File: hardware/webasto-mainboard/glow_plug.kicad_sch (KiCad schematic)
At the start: 23 parts, among them Q10 SSM3J374R, Q11 2N7002, Q12 SUD50P04-08, Q13 SUD50P04-08, Q14 SUD50P04-08, Q15 SUD50P04-08, Q16 SUD50P04-08, Q17 2N7002, Q18 2N7002, U6 LM7805_TO220, U7 INA219BxDCN

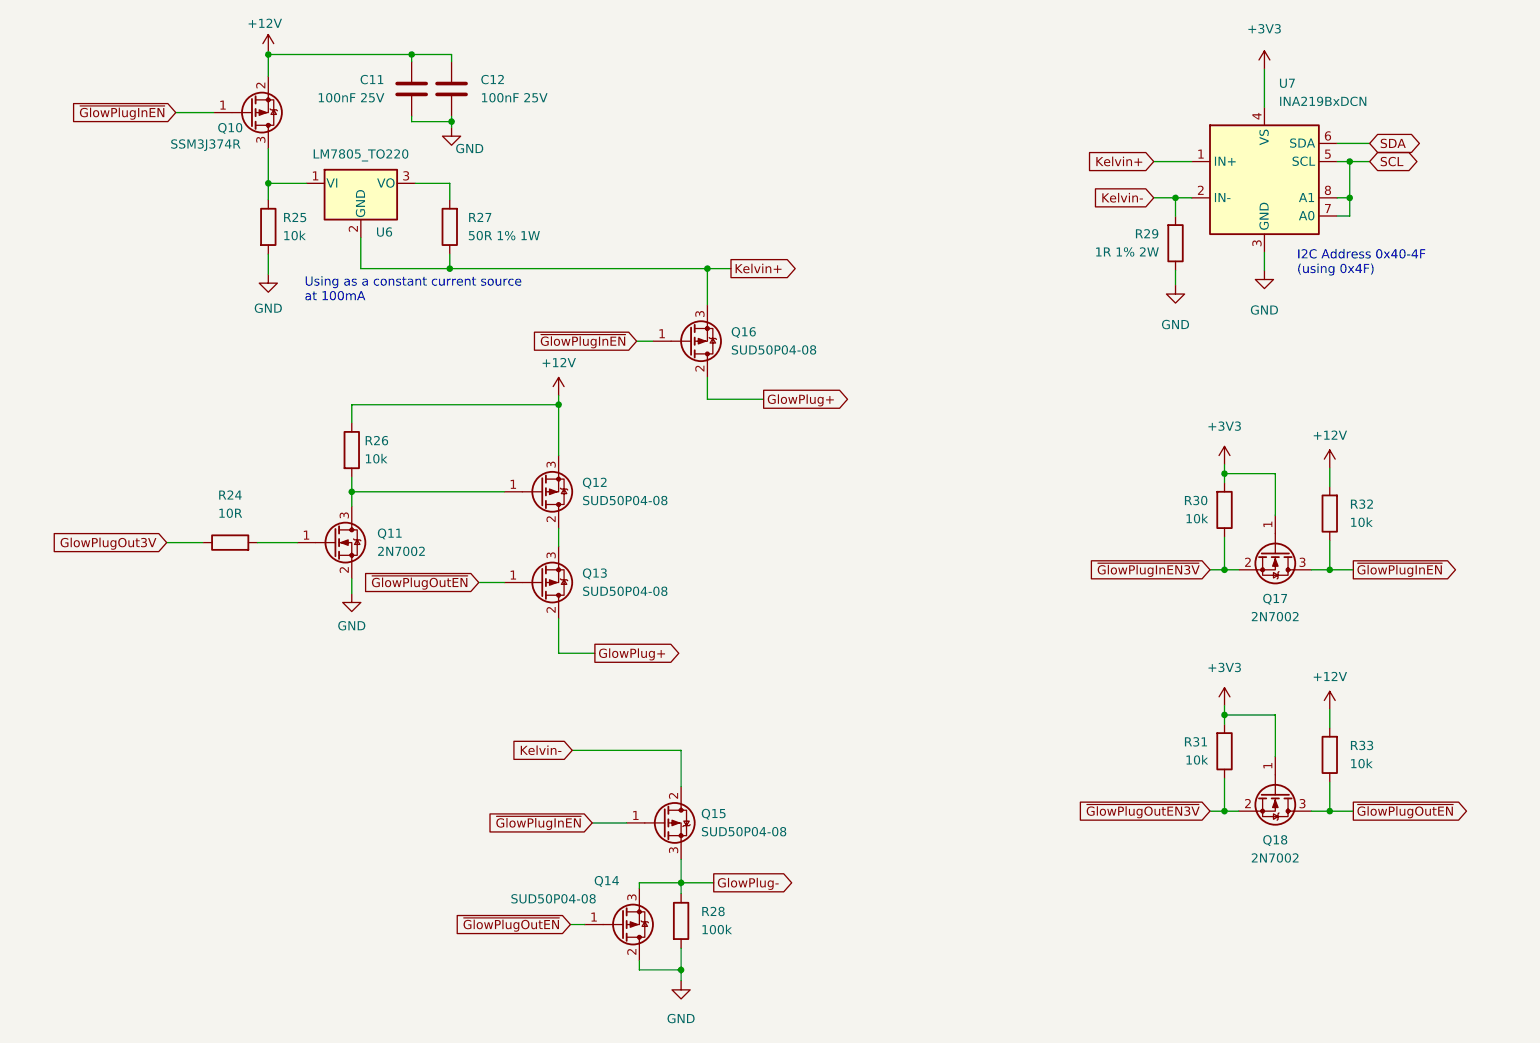
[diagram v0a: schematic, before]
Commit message: Oops.  StartRun is active at +12V.  Change the level translation.
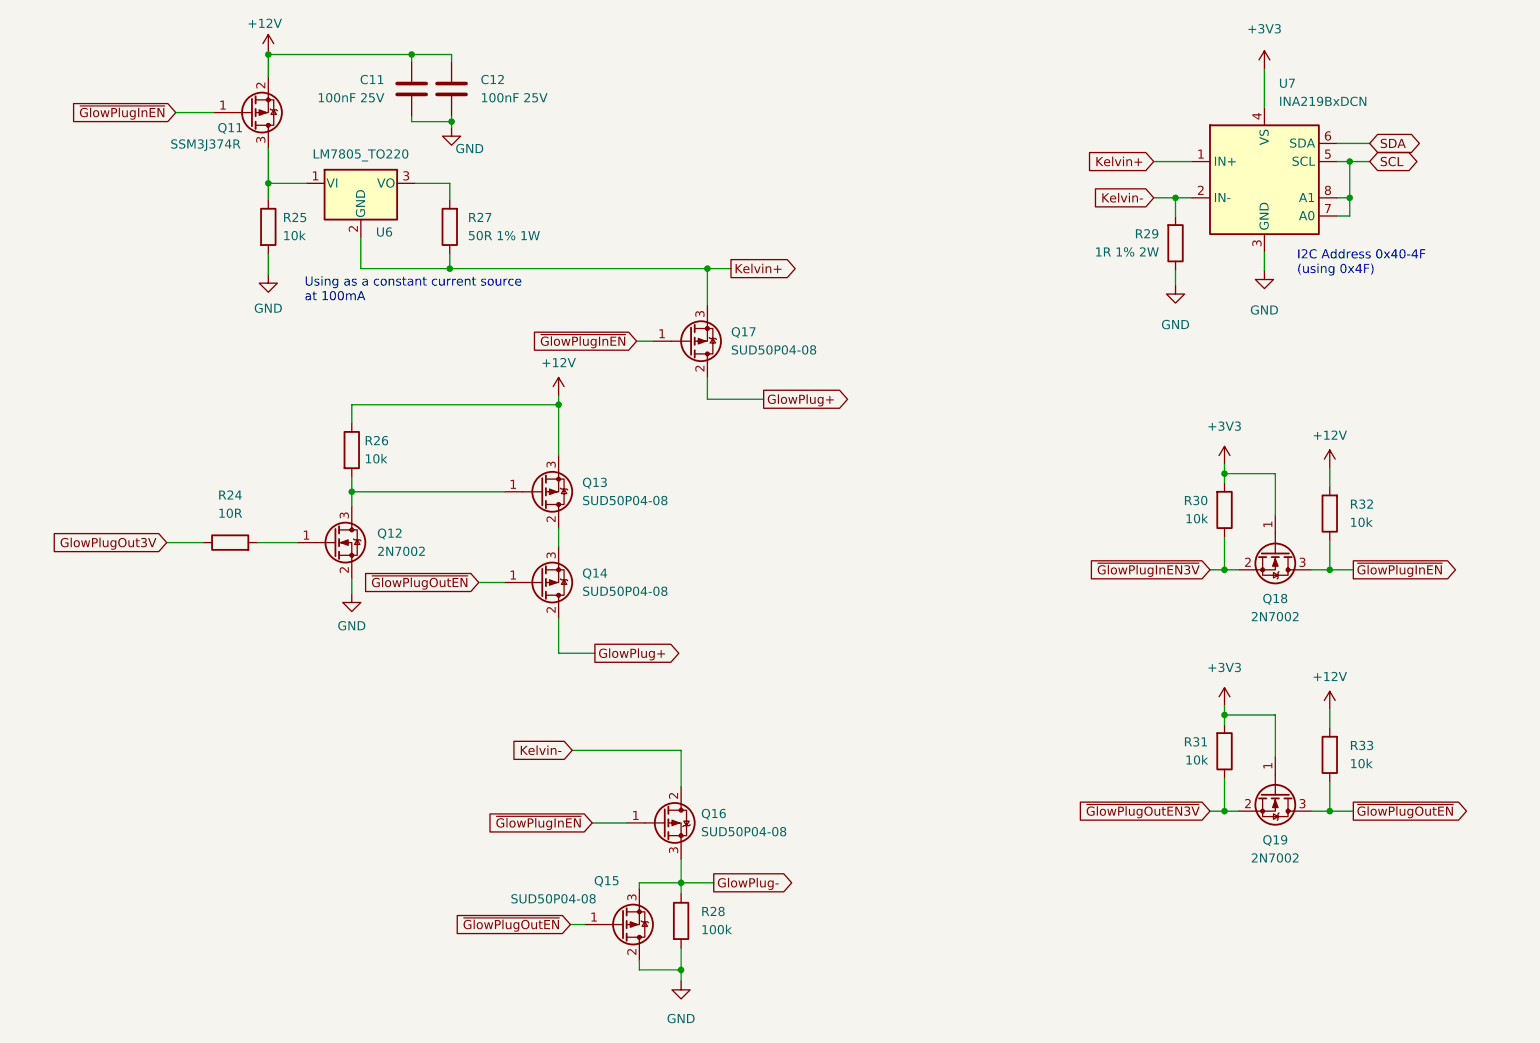
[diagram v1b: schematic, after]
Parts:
- renumbered Q10 to Q11, Q11 to Q12, Q12 to Q13, Q13 to Q14, Q14 to Q15, Q15 to Q16, Q16 to Q17, Q17 to Q18, Q18 to Q19
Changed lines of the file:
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@@
   (symbol (lib_id "Transistor_FET:2N7002") (at 204.089 97.536 270) (unit 1)
     (in_bom yes) (on_board yes) (fields_autoplaced)
-    (property "Reference" "Q17" (id 0) (at 204.089 104.14 90))
+    (property "Reference" "Q18" (id 0) (at 204.089 104.14 90))
     (property "Value" "2N7002" (id 1) (at 204.089 106.68 90))
     (property "Footprint" "Package_TO_SOT_SMD:SOT-23" (id 2) (at 202.184 102.616 0)
@@
   (symbol (lib_name "+3V3_1") (lib_id "power:+3V3") (at 202.565 29.972 0) (unit 1)
     (in_bom yes) (on_board yes) (fields_autoplaced)
-    (property "Reference" "#PWR062" (id 0) (at 202.565 33.782 0)
+    (property "Reference" "#PWR063" (id 0) (at 202.565 33.782 0)
       (effects (font (size 1.27 1.27)) hide)
     )
@@
   (symbol (lib_name "GND_8") (lib_id "power:GND") (at 202.565 58.166 0) (unit 1)
     (in_bom yes) (on_board yes) (fields_autoplaced)
-    (property "Reference" "#PWR063" (id 0) (at 202.565 64.516 0)
+    (property "Reference" "#PWR064" (id 0) (at 202.565 64.516 0)
       (effects (font (size 1.27 1.27)) hide)
     )
@@
   (symbol (lib_id "Transistor_FET:SUD50P04-08") (at 122.047 68.072 0) (mirror x) (unit 1)
     (in_bom yes) (on_board yes) (fields_autoplaced)
-    (property "Reference" "Q16" (id 0) (at 127.889 66.8019 0)
+    (property "Reference" "Q17" (id 0) (at 127.889 66.8019 0)
       (effects (font (size 1.27 1.27)) (justify left))
     )
@@
   (symbol (lib_name "+3V3_2") (lib_id "power:+3V3") (at 196.977 85.344 0) (unit 1)
     (in_bom yes) (on_board yes) (fields_autoplaced)
-    (property "Reference" "#PWR060" (id 0) (at 196.977 89.154 0)
+    (property "Reference" "#PWR061" (id 0) (at 196.977 89.154 0)
       (effects (font (size 1.27 1.27)) hide)
     )
@@
   (symbol (lib_name "GND_2") (lib_id "power:GND") (at 74.803 103.378 0) (unit 1)
     (in_bom yes) (on_board yes) (fields_autoplaced)
-    (property "Reference" "#PWR055" (id 0) (at 74.803 109.728 0)
+    (property "Reference" "#PWR056" (id 0) (at 74.803 109.728 0)
       (effects (font (size 1.27 1.27)) hide)
     )
@@
   (symbol (lib_name "+3V3_2") (lib_id "power:+3V3") (at 196.977 119.126 0) (unit 1)
     (in_bom yes) (on_board yes) (fields_autoplaced)
-    (property "Reference" "#PWR061" (id 0) (at 196.977 122.936 0)
+    (property "Reference" "#PWR062" (id 0) (at 196.977 122.936 0)
       (effects (font (size 1.27 1.27)) hide)
     )
@@
   (symbol (lib_id "Transistor_FET:SUD50P04-08") (at 118.364 135.509 0) (unit 1)
     (in_bom yes) (on_board yes) (fields_autoplaced)
-    (property "Reference" "Q15" (id 0) (at 123.698 134.2389 0)
+    (property "Reference" "Q16" (id 0) (at 123.698 134.2389 0)
       (effects (font (size 1.27 1.27)) (justify left))
     )
@@
   (symbol (lib_id "Transistor_FET:2N7002") (at 204.089 131.318 270) (unit 1)
     (in_bom yes) (on_board yes) (fields_autoplaced)
-    (property "Reference" "Q18" (id 0) (at 204.089 137.922 90))
+    (property "Reference" "Q19" (id 0) (at 204.089 137.922 90))
     (property "Value" "2N7002" (id 1) (at 204.089 140.462 90))
     (property "Footprint" "Package_TO_SOT_SMD:SOT-23" (id 2) (at 202.184 136.398 0)
@@
   (symbol (lib_name "GND_9") (lib_id "power:GND") (at 120.904 157.607 0) (unit 1)
     (in_bom yes) (on_board yes) (fields_autoplaced)
-    (property "Reference" "#PWR058" (id 0) (at 120.904 163.957 0)
+    (property "Reference" "#PWR059" (id 0) (at 120.904 163.957 0)
       (effects (font (size 1.27 1.27)) hide)
     )
@@
   (symbol (lib_name "+12V_3") (lib_id "power:+12V") (at 211.709 85.852 0) (unit 1)
     (in_bom yes) (on_board yes) (fields_autoplaced)
-    (property "Reference" "#PWR064" (id 0) (at 211.709 89.662 0)
+    (property "Reference" "#PWR065" (id 0) (at 211.709 89.662 0)
       (effects (font (size 1.27 1.27)) hide)
     )
@@
   (symbol (lib_name "GND_5") (lib_id "power:GND") (at 88.773 38.1 0) (unit 1)
     (in_bom yes) (on_board yes)
-    (property "Reference" "#PWR056" (id 0) (at 88.773 44.45 0)
+    (property "Reference" "#PWR057" (id 0) (at 88.773 44.45 0)
       (effects (font (size 1.27 1.27)) hide)
     )
@@
   (symbol (lib_name "GND_8") (lib_id "power:GND") (at 190.119 60.198 0) (unit 1)
     (in_bom yes) (on_board yes) (fields_autoplaced)
-    (property "Reference" "#PWR059" (id 0) (at 190.119 66.548 0)
+    (property "Reference" "#PWR060" (id 0) (at 190.119 66.548 0)
       (effects (font (size 1.27 1.27)) hide)
     )
@@
   (symbol (lib_id "Transistor_FET:SUD50P04-08") (at 101.219 89.154 0) (mirror x) (unit 1)
     (in_bom yes) (on_board yes) (fields_autoplaced)
-    (property "Reference" "Q12" (id 0) (at 107.061 87.8839 0)
+    (property "Reference" "Q13" (id 0) (at 107.061 87.8839 0)
       (effects (font (size 1.27 1.27)) (justify left))
     )
@@
   (symbol (lib_name "+12V_2") (lib_id "power:+12V") (at 63.119 27.686 0) (unit 1)
     (in_bom yes) (on_board yes)
-    (property "Reference" "#PWR053" (id 0) (at 63.119 31.496 0)
+    (property "Reference" "#PWR054" (id 0) (at 63.119 31.496 0)
       (effects (font (size 1.27 1.27)) hide)
     )
@@
   (symbol (lib_name "+12V_3") (lib_id "power:+12V") (at 211.709 119.634 0) (unit 1)
     (in_bom yes) (on_board yes) (fields_autoplaced)
-    (property "Reference" "#PWR065" (id 0) (at 211.709 123.444 0)
+    (property "Reference" "#PWR066" (id 0) (at 211.709 123.444 0)
       (effects (font (size 1.27 1.27)) hide)
     )
@@
   (symbol (lib_id "Transistor_FET:SUD50P04-08") (at 112.522 149.733 0) (mirror x) (unit 1)
     (in_bom yes) (on_board yes)
-    (property "Reference" "Q14" (id 0) (at 108.712 143.637 0)
+    (property "Reference" "Q15" (id 0) (at 108.712 143.637 0)
       (effects (font (size 1.27 1.27)) (justify left))
     )
@@
   (symbol (lib_name "GND_3") (lib_id "power:GND") (at 63.119 58.674 0) (unit 1)
     (in_bom yes) (on_board yes) (fields_autoplaced)
-    (property "Reference" "#PWR054" (id 0) (at 63.119 65.024 0)
+    (property "Reference" "#PWR055" (id 0) (at 63.119 65.024 0)
       (effects (font (size 1.27 1.27)) hide)
     )
@@
   (symbol (lib_id "Transistor_FET:AO3401A") (at 60.579 36.068 0) (mirror x) (unit 1)
     (in_bom yes) (on_board yes)
-    (property "Reference" "Q10" (id 0) (at 56.007 38.227 0)
+    (property "Reference" "Q11" (id 0) (at 56.007 38.227 0)
       (effects (font (size 1.27 1.27)) (justify left))
     )
@@
   (symbol (lib_id "Transistor_FET:2N7002") (at 72.263 96.266 0) (unit 1)
     (in_bom yes) (on_board yes) (fields_autoplaced)
-    (property "Reference" "Q11" (id 0) (at 78.359 94.9959 0)
+    (property "Reference" "Q12" (id 0) (at 78.359 94.9959 0)
       (effects (font (size 1.27 1.27)) (justify left))
     )
@@
   (symbol (lib_name "+12V_1") (lib_id "power:+12V") (at 103.759 75.692 0) (unit 1)
     (in_bom yes) (on_board yes) (fields_autoplaced)
-    (property "Reference" "#PWR057" (id 0) (at 103.759 79.502 0)
+    (property "Reference" "#PWR058" (id 0) (at 103.759 79.502 0)
       (effects (font (size 1.27 1.27)) hide)
     )
@@
   (symbol (lib_id "Transistor_FET:SUD50P04-08") (at 101.219 101.854 0) (mirror x) (unit 1)
     (in_bom yes) (on_board yes) (fields_autoplaced)
-    (property "Reference" "Q13" (id 0) (at 107.061 100.5839 0)
-      (effects (font (size 1.27 1.27)) (justify left))
-    )
+    (property "Reference" "Q14" (id 0) (at 107.061 100.5839 0)
+      (effects (font (size 1.27 1.27)) (justify left))
+    )
